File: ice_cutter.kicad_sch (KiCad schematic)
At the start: 148 parts, among them J1 Conn_01x01_Male, J2 Barrel_Jack, J3 pot, J4 Conn_01x01_Male, J5 program, J6 program2, J7 hands, J8 UART, J9 xt60, M1 Motor_Servo, M2 Motor_Servo, Q1 Q_PMOS_GSD, Q11 Q_NMOS_GSD, Q12 Q_NMOS_GSD, Q13 Q_NMOS_GSD, Q14 Q_NMOS_GSD, Q2 Q_PMOS_GSD, Q3 Q_PMOS_GSD, Q4 S8550, Q5 Q_NMOS_GSD, Q7 Q_NMOS_GSD, SW1 SW_Push, SW2 SW_Push, SW3 SW_Push, U1 LM317_TO-252, U10 TMP117, U11 TM1620, U12 INA219AxD, U2 LM317_TO-252, U3 INA219AxD, U4 LM317_TO-252, U5 INA219AxD, U6 FJ4301AH, U7 FJ4301AH, U8 STM32G030XX, U9 SHT30-DIS

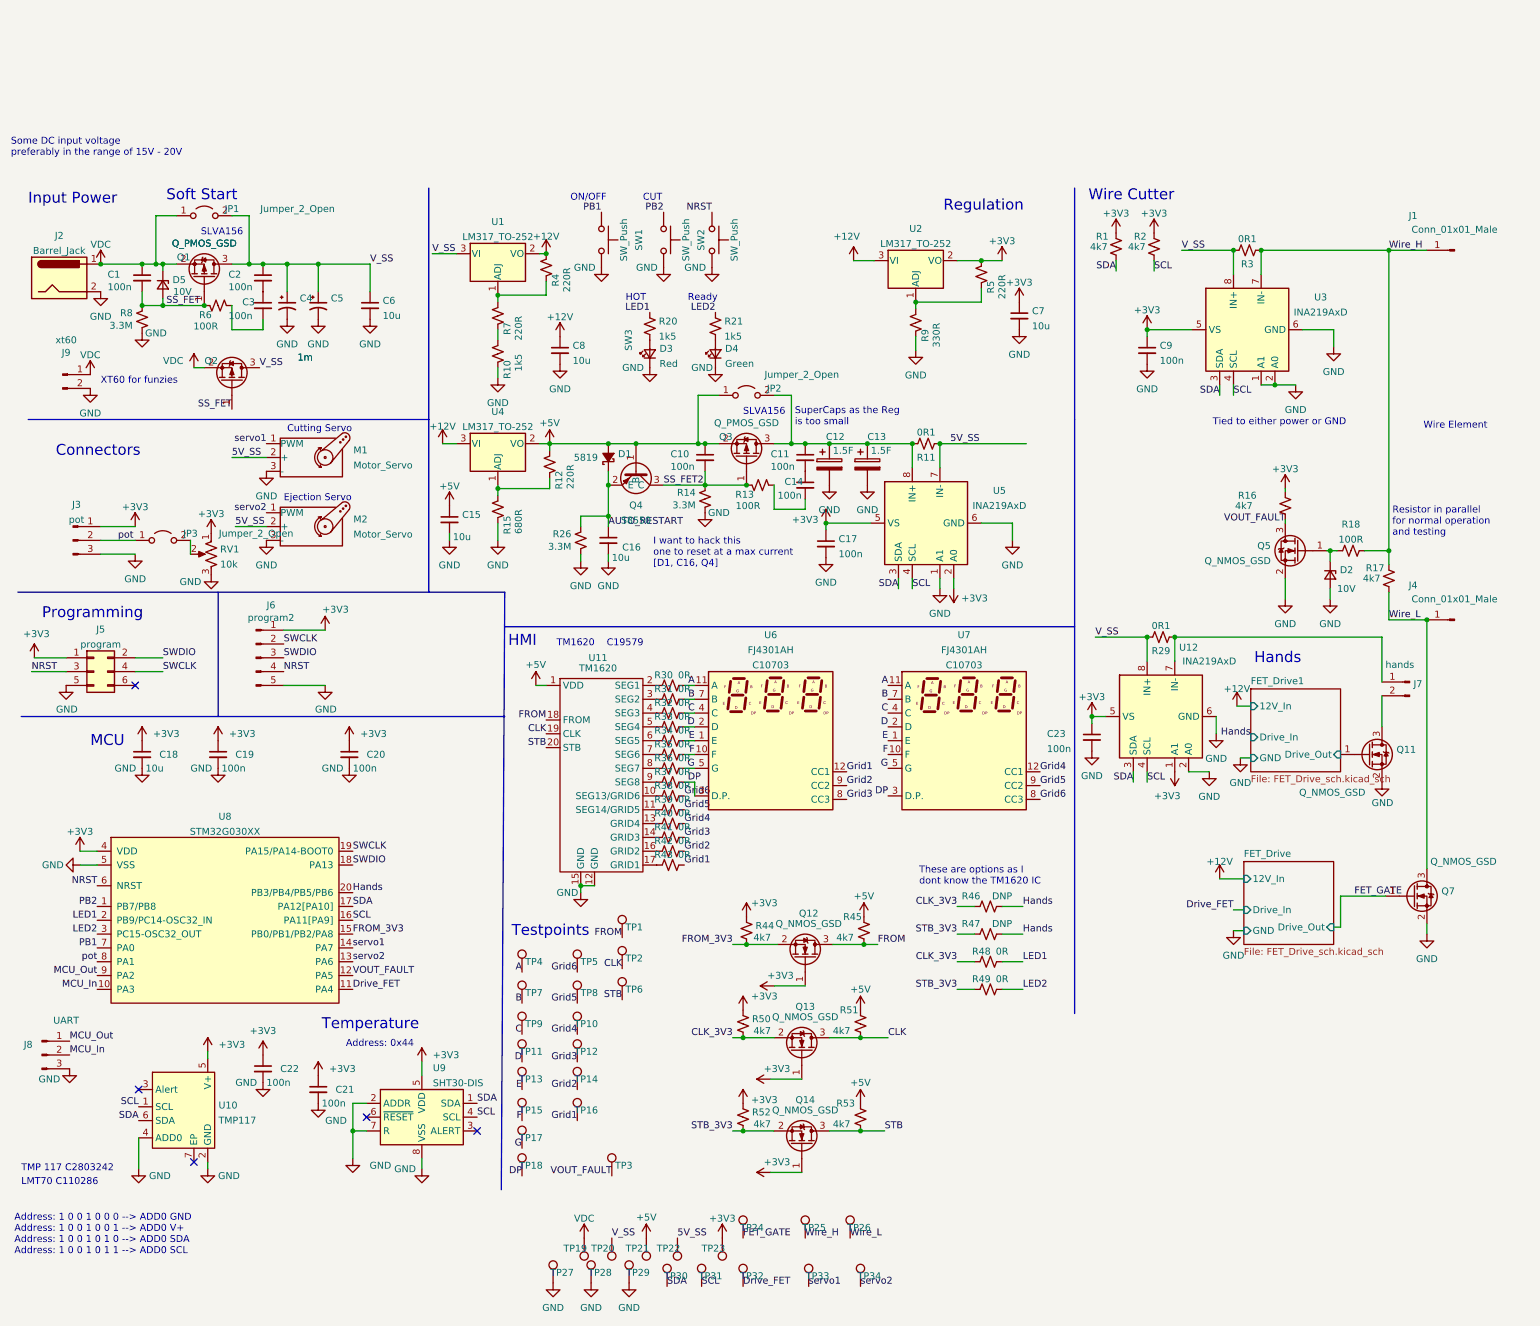
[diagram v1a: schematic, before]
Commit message: got lazy, went 4 layer. Some of layer 3 done. progressing. Mainly committing for board chronological how to sake. Added Caps on the TM1620
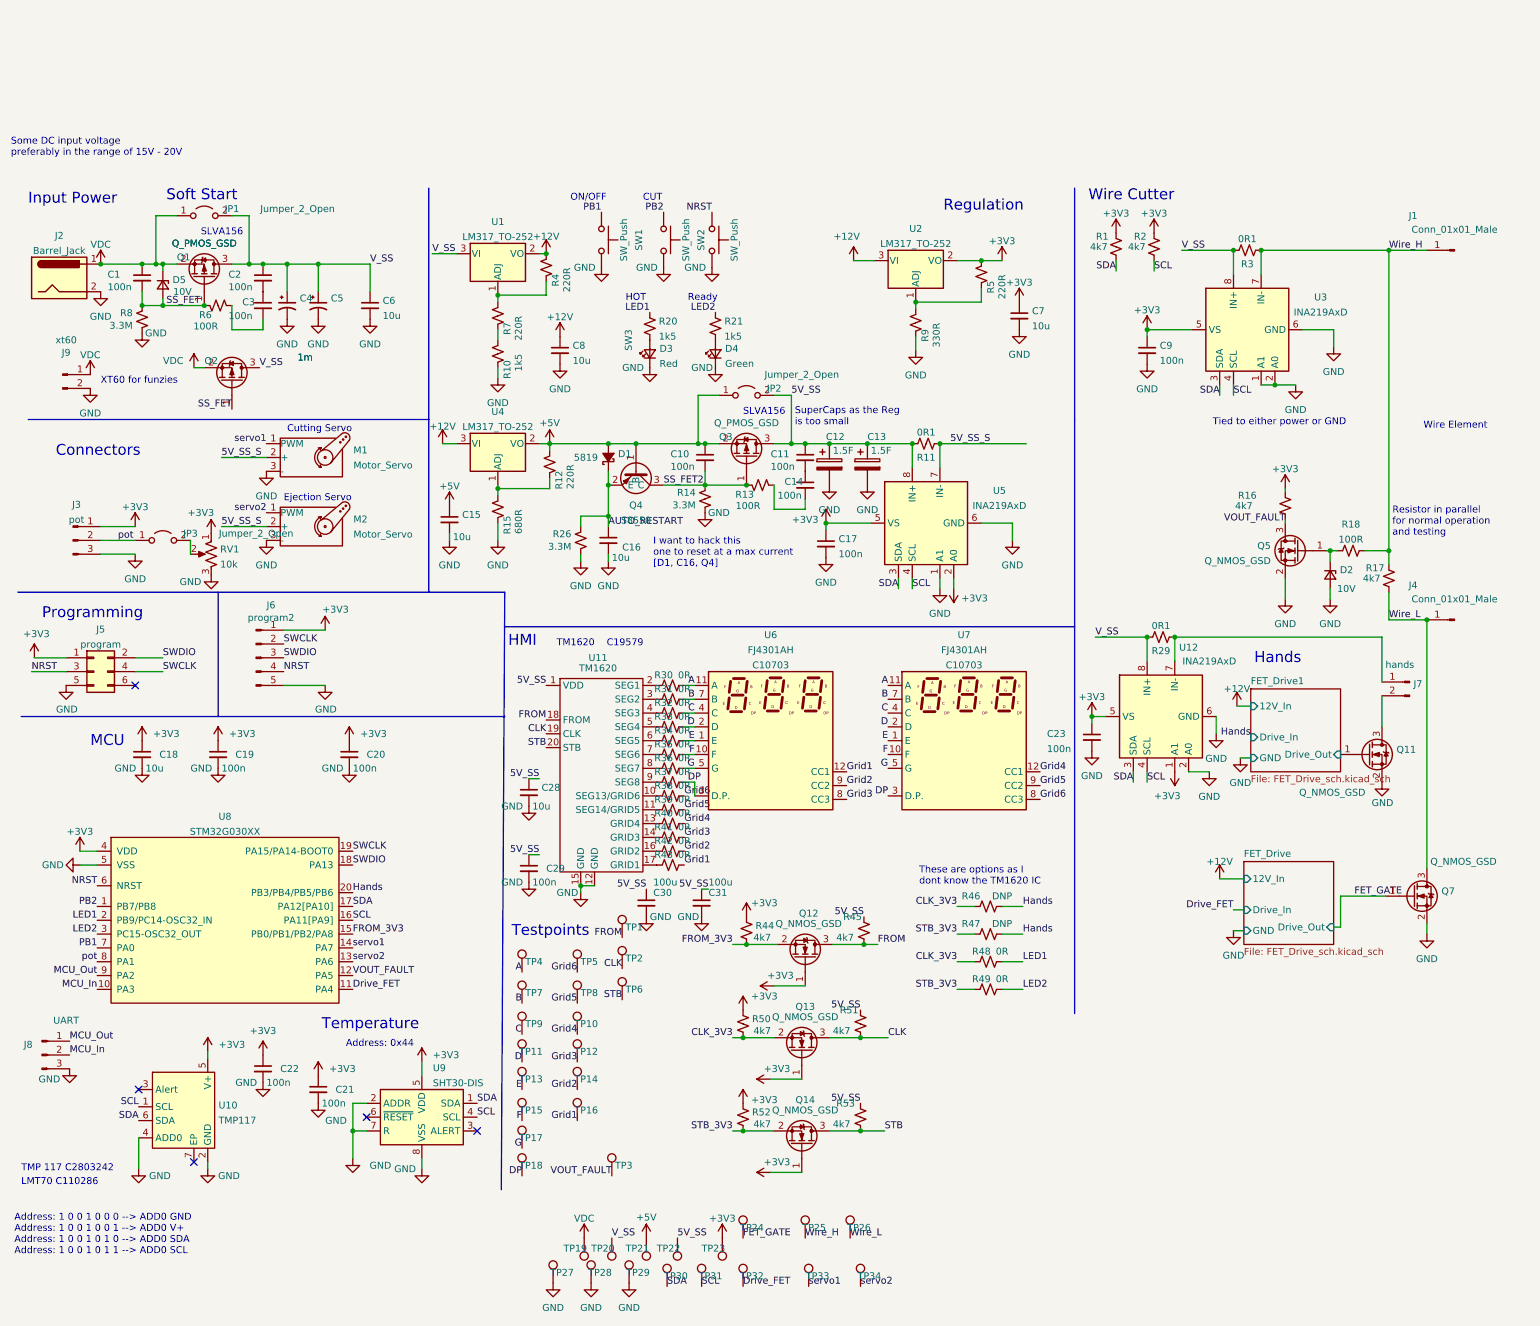
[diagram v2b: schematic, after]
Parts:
- added C28: 10u, Capacitor_SMD:C_0603_1608Metric, symbol Device:C_Small
- added C29: 100n, Capacitor_SMD:C_0402_1005Metric, symbol Device:C_Small
- added C30, C31: 100u, Capacitor_SMD:C_1206_3216Metric_Pad1.33x1.80mm_HandSolder, symbol Device:C_Small
- D1: LCSC C963381 -> C963381
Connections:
- net +5V: no longer R45.2, R51.2, R53.2, U11.1 (VDD)
- net 5V_SS: now also C11.1, C12.1, C13.1, JP2.2 (B), Q3.3 (D), R11.1, R45.2, R51.2, R53.2, U11.1 (VDD), U5.8 (IN+), C28.1, C29.1, C30.1, C31.1; no longer M1.2 (+), M2.2 (+), R11.2, U5.7 (IN-)
- net GND: now also C28.2, C29.2, C30.2, C31.2
- new net 5V_SS_S: M1.2 (+), M2.2 (+), R11.2, U5.7 (IN-)

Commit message: improved schematic and changed the shunt resistors
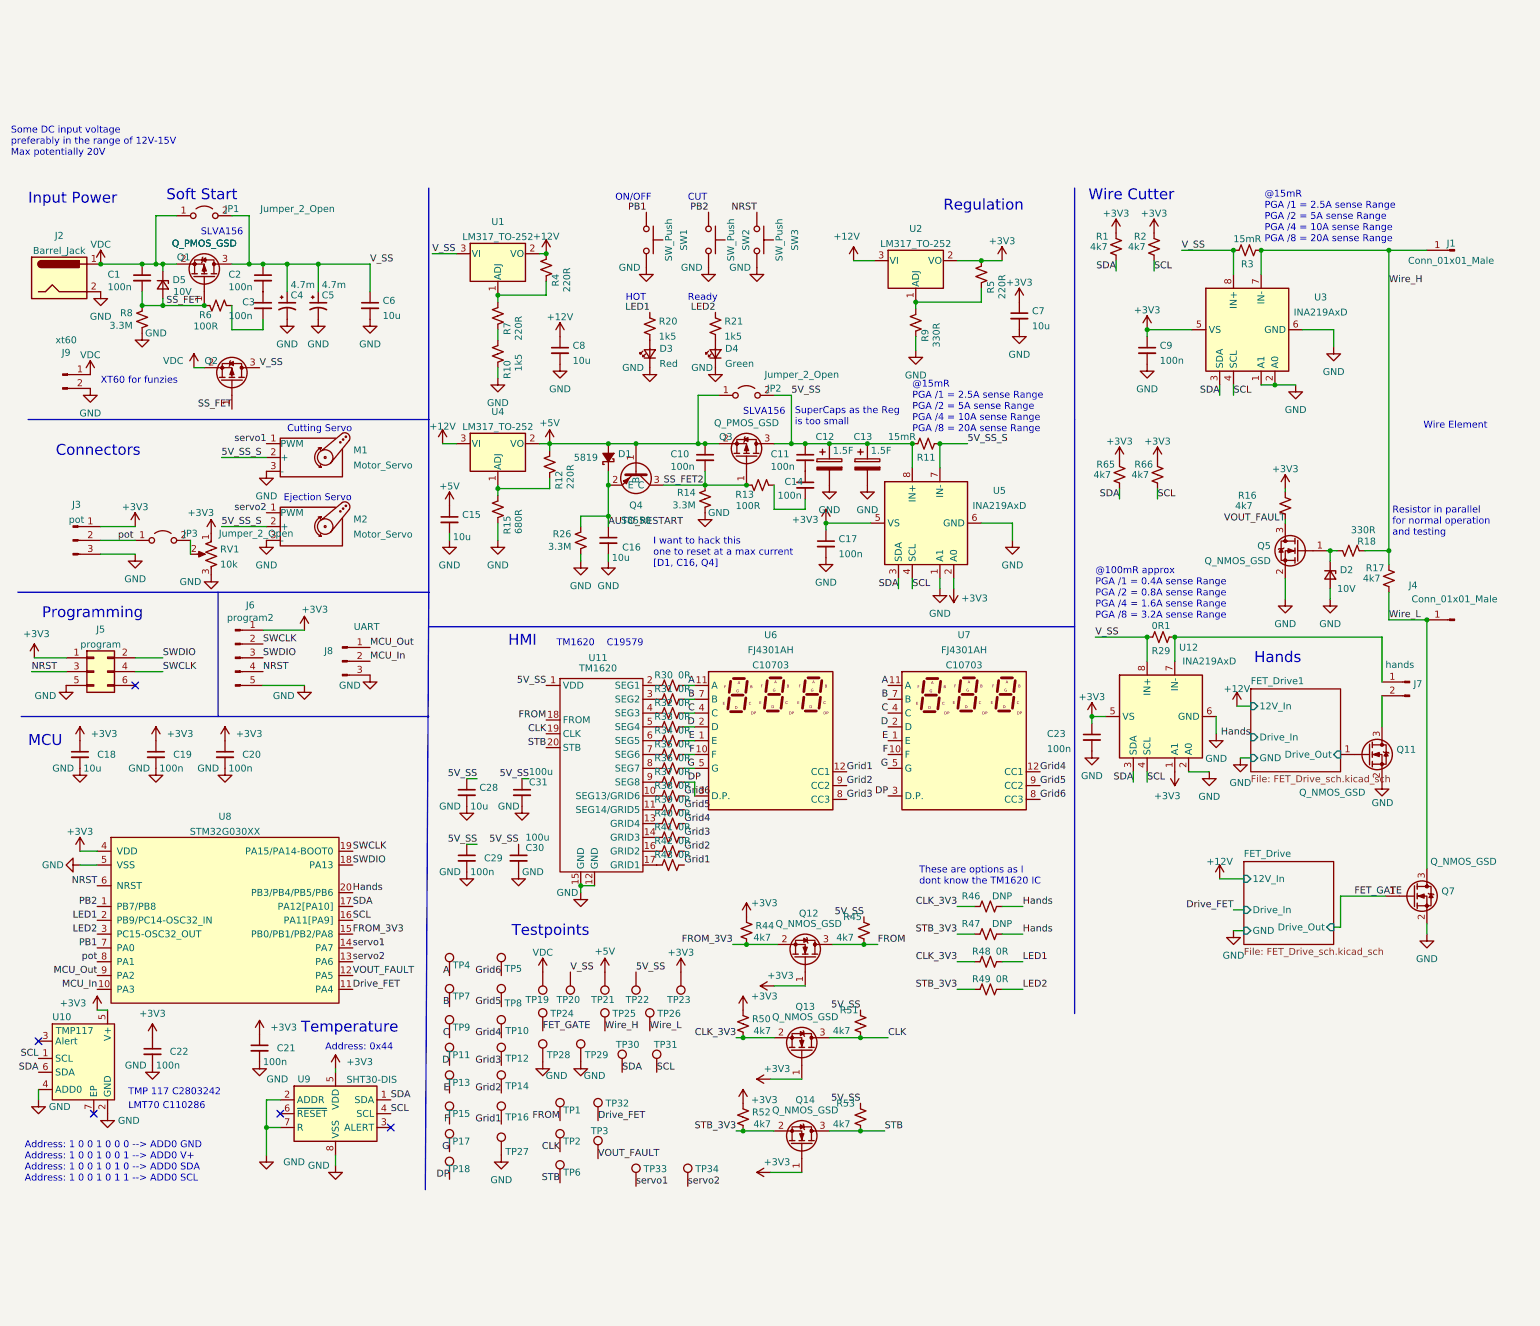
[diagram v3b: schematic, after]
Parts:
- added R65, R66: 4k7, Resistor_SMD:R_0402_1005Metric, symbol Device:R_Small_US
- C4, C5: value 1m -> 4.7m
- R11, R3: value 0R1 -> 15mR; footprint Resistor_SMD:R_1206_3216Metric -> Resistor_SMD:R_2512_6332Metric; Extended 0 -> 1; LCSC C25334 -> C105381; Price 0.0087 -> 0.087
- R18: value 100R -> 330R; LCSC C25076 -> C25104
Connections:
- net +3V3: now also R65.2, R66.2
- net SCL: now also R66.1
- net SDA: now also R65.1
- net Wire_H: now also R18.1; no longer R18.2
- net at D2.1 (K), Q5.1 (G): now also R18.2; no longer R18.1
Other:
- note added: "@100mR approx PGA /1 = 0.4A sense Range PGA /2 = 0.8A sense Range PGA /4 = 1.6A sense Range PGA /8 = 3.2A sense Range"
- note added: "@15mR PGA /1 = 2.5A sense Range PGA /2 = 5A sense Range PGA /4 = 10A sense Range PGA /8 = 20A sense Range"
- note added: "Some DC input voltage preferably in the range of 12V-15V Max potentially 20V"
- note removed: "Some DC input voltage preferably in the range of 15V - 20V"
- note removed: "Tied to either power or GND"
- moved on the sheet: C18, C19, C20, C21, C22, C28, C29, C30, C31, J6, J8, SW1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

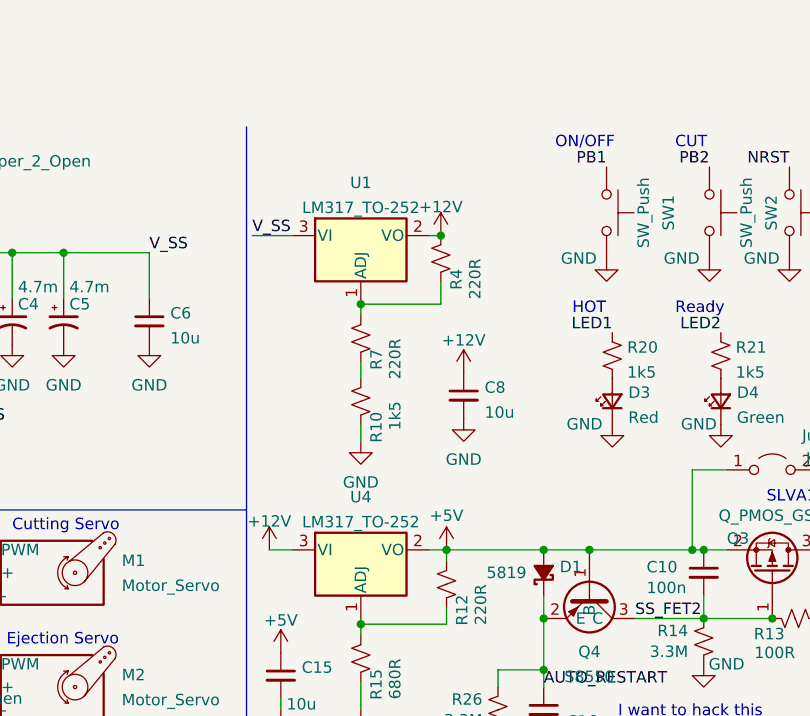
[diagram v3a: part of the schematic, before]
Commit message: modified the system to operate on 5V - bypassed all regs and changed the BIG FET to a lower threshold V
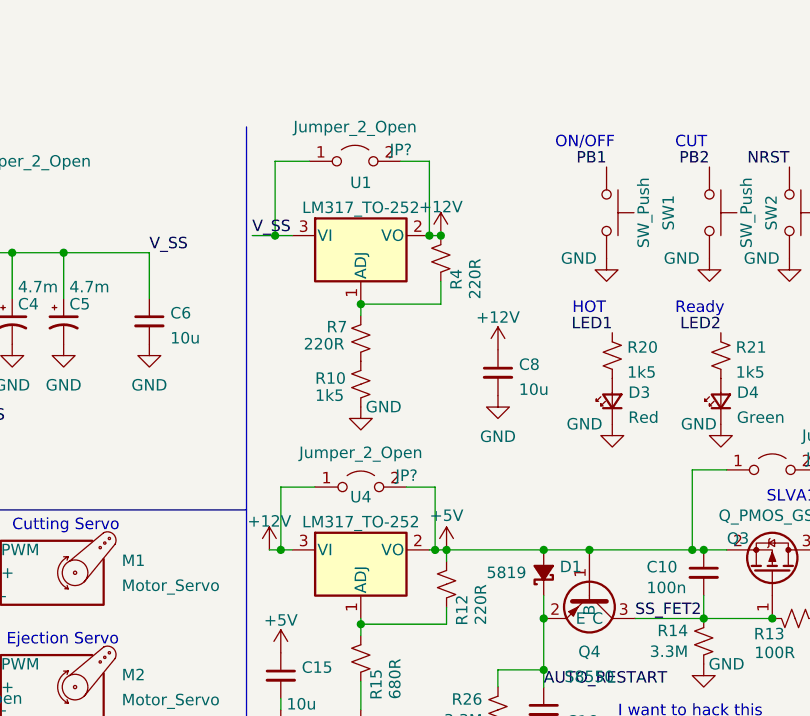
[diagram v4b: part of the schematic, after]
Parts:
- added JP? (x2): Jumper_2_Open, Jumper:SolderJumper-2_P1.3mm_Open_RoundedPad1.0x1.5mm, symbol Jumper:Jumper_2_Open
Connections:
- net +12V: now also JP?.1 (A), JP?.2 (B)
- net +5V: now also JP?.2 (B)
- net V_SS: now also JP?.1 (A)
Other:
- moved on the sheet: C8, R10
